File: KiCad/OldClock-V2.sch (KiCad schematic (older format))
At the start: 40 parts, among them J1 FaseCTRL, J2 Screw_Terminal_1x02, J3 Screw_Terminal_1x02, J4 Screw_Terminal_1x02, K1 FINDER-32.21-x300, Q1 Q_NPN_CBE, Q2 Q_PNP_CBE, Q3 Q_PNP_BCE, Q4 Q_NPN_CBE, SW1 Dw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

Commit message: Schematical update
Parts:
- removed K1: FINDER-32.21-x300, Relays_THT:Relay_SPST_Finder_32.21-x300, symbol FINDER-32.21-x300
- added R11: 220R, symbol R
- D7: value LED -> LED_V
- D8: value LED -> LED_R
- Q1: value Q_NPN_CBE -> BC547
- Q2: value Q_PNP_CBE -> BC327
- Q4: value Q_NPN_CBE -> BD410
- R1, R10: value R -> 220R
- R2: value R -> 10k
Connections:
- net +12V: now also J2.2
- net GND: now also Q4.3 (E); no longer Q4.1 (C)
- net at SH1.10 ((*)_10): no longer D8.2 (A)
- net at SH1.11 ((*/MOSI)_11): now also R10.1
- net at SH1.12 ((MISO)_12): no longer R10.1
- net at SH1.13 ((SCK)_13): now also D8.2 (A)
- net at J2.1: now also Q4.1 (C)
- net at Q2.2 (B), R2.1: now also R11.1; no longer Q1.1 (C)
- new net: Q1.1 (C), R11.2
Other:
- moved on the sheet: D8, J2, Q1, Q4, R1, R10, R8
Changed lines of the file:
@@
 LIBS:nxp
 LIBS:dc-dc
-LIBS:OdlClock-V2-cache
+LIBS:OldClock-V2-cache
 EELAYER 25 0
 EELAYER END
@@
 L Q_NPN_CBE Q4
 U 1 1 5A37E50C
-P 8850 1175
-F 0 "Q4" H 9050 1225 50  0000 L CNN
-F 1 "Q_NPN_CBE" H 9050 1125 50  0000 L CNN
-F 2 "" H 9050 1275 50  0001 C CNN
-F 3 "" H 8850 1175 50  0001 C CNN
-	1    8850 1175
+P 8875 1725
+F 0 "Q4" H 9075 1775 50  0000 L CNN
+F 1 "BD410" H 9125 1525 50  0000 L CNN
+F 2 "" H 9075 1825 50  0001 C CNN
+F 3 "" H 8875 1725 50  0001 C CNN
+	1    8875 1725
 	1    0    0    -1
 $EndComp
@@
 L R R10
 U 1 1 5A37E57D
-P 8500 1175
-F 0 "R10" V 8580 1175 50  0000 C CNN
-F 1 "R" V 8500 1175 50  0000 C CNN
-F 2 "" V 8430 1175 50  0001 C CNN
-F 3 "" H 8500 1175 50  0001 C CNN
-	1    8500 1175
+P 8525 1725
+F 0 "R10" V 8605 1725 50  0000 C CNN
+F 1 "220R" V 8525 1725 50  0000 C CNN
+F 2 "" V 8455 1725 50  0001 C CNN
+F 3 "" H 8525 1725 50  0001 C CNN
+	1    8525 1725
 	0    -1   -1   0
 $EndComp
@@
 L GND #PWR29
 U 1 1 5A37E9D1
-P 8950 975
-F 0 "#PWR29" H 8950 725 50  0001 C CNN
-F 1 "GND" H 8950 825 50  0000 C CNN
-F 2 "" H 8950 975 50  0001 C CNN
-F 3 "" H 8950 975 50  0001 C CNN
-	1    8950 975
-	-1   0    0    1
+P 8975 1925
+F 0 "#PWR29" H 8975 1675 50  0001 C CNN
+F 1 "GND" H 8975 1775 50  0000 C CNN
+F 2 "" H 8975 1925 50  0001 C CNN
+F 3 "" H 8975 1925 50  0001 C CNN
+	1    8975 1925
+	1    0    0    -1
 $EndComp
 $Comp
 L +12V #PWR30
 U 1 1 5A37EA62
-P 8950 1975
-F 0 "#PWR30" H 8950 1825 50  0001 C CNN
-F 1 "+12V" H 8950 2115 50  0000 C CNN
-F 2 "" H 8950 1975 50  0001 C CNN
-F 3 "" H 8950 1975 50  0001 C CNN
-	1    8950 1975
-	-1   0    0    1
-$EndComp
-$Comp
-L FINDER-32.21-x300 K1
-U 1 1 5A37FBE9
-P 9150 1675
-F 0 "K1" H 9600 1825 50  0000 L CNN
-F 1 "FINDER-32.21-x300" H 9600 1725 50  0000 L CNN
-F 2 "Relays_THT:Relay_SPST_Finder_32.21-x300" H 10420 1645 50  0001 C CNN
-F 3 "" H 9150 1675 50  0001 C CNN
-	1    9150 1675
-	1    0    0    -1
+P 9650 1100
+F 0 "#PWR30" H 9650 950 50  0001 C CNN
+F 1 "+12V" H 9650 1240 50  0000 C CNN
+F 2 "" H 9650 1100 50  0001 C CNN
+F 3 "" H 9650 1100 50  0001 C CNN
+	1    9650 1100
+	0    -1   -1   0
 $EndComp
 $Comp
 L Screw_Terminal_1x02 J2
 U 1 1 5A380BD8
-P 10550 1650
-F 0 "J2" H 10550 1900 50  0000 C TNN
-F 1 "Screw_Terminal_1x02" V 10400 1650 50  0000 C TNN
-F 2 "" H 10550 1425 50  0001 C CNN
-F 3 "" H 10525 1650 50  0001 C CNN
-	1    10550 1650
+P 9850 1200
+F 0 "J2" H 9850 1450 50  0000 C TNN
+F 1 "Screw_Terminal_1x02" V 9700 1200 50  0000 C TNN
+F 2 "" H 9850 975 50  0001 C CNN
+F 3 "" H 9825 1200 50  0001 C CNN
+	1    9850 1200
 	-1   0    0    1
 $EndComp
-Wire Wire Line
-	10350 1750 10350 2025
-Wire Wire Line
-	10350 2025 9350 2025
-Wire Wire Line
-	9350 2025 9350 1975
-Wire Wire Line
-	9450 1375 10250 1375
-Wire Wire Line
-	10250 1375 10250 1550
-Wire Wire Line
-	10250 1550 10350 1550
 $Comp
 L LED D7
@@
 P 6925 1975
 F 0 "D7" H 6925 2075 50  0000 C CNN
-F 1 "LED" H 6925 1875 50  0000 C CNN
+F 1 "LED_V" H 6925 1875 50  0000 C CNN
 F 2 "" H 6925 1975 50  0001 C CNN
 F 3 "" H 6925 1975 50  0001 C CNN
@@
 L LED D8
 U 1 1 5A381040
-P 7250 1850
-F 0 "D8" H 7250 1950 50  0000 C CNN
-F 1 "LED" H 7250 1750 50  0000 C CNN
-F 2 "" H 7250 1850 50  0001 C CNN
-F 3 "" H 7250 1850 50  0001 C CNN
-	1    7250 1850
+P 7250 1475
+F 0 "D8" H 7250 1575 50  0000 C CNN
+F 1 "LED_R" H 7250 1375 50  0000 C CNN
+F 2 "" H 7250 1475 50  0001 C CNN
+F 3 "" H 7250 1475 50  0001 C CNN
+	1    7250 1475
 	-1   0    0    1
 $EndComp
 Wire Wire Line
-	7100 1850 6775 1850
+	7100 1475 6775 1475
 Wire Wire Line
 	7400 1975 7075 1975
@@
 L R R8
 U 1 1 5A3814AB
-P 7550 1850
-F 0 "R8" V 7630 1850 50  0000 C CNN
-F 1 "R" V 7550 1850 50  0000 C CNN
-F 2 "" V 7480 1850 50  0001 C CNN
-F 3 "" H 7550 1850 50  0001 C CNN
-	1    7550 1850
+P 7550 1475
+F 0 "R8" V 7630 1475 50  0000 C CNN
+F 1 "R" V 7550 1475 50  0000 C CNN
+F 2 "" V 7480 1475 50  0001 C CNN
+F 3 "" H 7550 1475 50  0001 C CNN
+	1    7550 1475
 	0    -1   -1   0
 $EndComp
@@
 	0    -1   -1   0
 $EndComp
-Wire Wire Line
-	7700 1975 7700 1850
 $Comp
 L CONN_01X02 J1
@@
 Text GLabel 6775 2100 2    60   Input ~ 0
 UPS
-Wire Wire Line
-	8350 1175 7200 1175
-Wire Wire Line
-	7200 1175 7200 1600
-Wire Wire Line
-	7200 1600 6775 1600
 $Comp
 L R R3
@@
 P 1875 2250
 F 0 "Q2" H 2075 2300 50  0000 L CNN
-F 1 "Q_PNP_CBE" H 2475 2625 50  0001 L CNN
+F 1 "BC327" H 1675 2400 50  0000 L CNN
 F 2 "" H 2075 2350 50  0001 C CNN
 F 3 "" H 1875 2250 50  0001 C CNN
@@
 L Q_NPN_CBE Q1
 U 1 1 5A875735
-P 1575 2450
-F 0 "Q1" H 1775 2500 50  0000 L CNN
-F 1 "Q_NPN_CBE" H 1300 2875 50  0000 L CNN
-F 2 "" H 1775 2550 50  0001 C CNN
-F 3 "" H 1575 2450 50  0001 C CNN
-	1    1575 2450
+P 1575 2750
+F 0 "Q1" H 1775 2800 50  0000 L CNN
+F 1 "BC547" H 1225 2825 50  0000 L CNN
+F 2 "" H 1775 2850 50  0001 C CNN
+F 3 "" H 1575 2750 50  0001 C CNN
+	1    1575 2750
 	1    0    0    -1
 $EndComp
@@
 P 1525 2250
 F 0 "R2" V 1605 2250 50  0000 C CNN
-F 1 "R" V 1525 2250 50  0000 C CNN
+F 1 "10k" V 1525 2250 50  0000 C CNN
 F 2 "" V 1455 2250 50  0001 C CNN
 F 3 "" H 1525 2250 50  0001 C CNN
@@
 L R R1
 U 1 1 5A875B9C
-P 1225 2450
-F 0 "R1" V 1305 2450 50  0000 C CNN
-F 1 "R" V 1225 2450 50  0000 C CNN
-F 2 "" V 1155 2450 50  0001 C CNN
-F 3 "" H 1225 2450 50  0001 C CNN
-	1    1225 2450
+P 1225 2750
+F 0 "R1" V 1305 2750 50  0000 C CNN
+F 1 "220R" V 1225 2750 50  0000 C CNN
+F 2 "" V 1155 2750 50  0001 C CNN
+F 3 "" H 1225 2750 50  0001 C CNN
+	1    1225 2750
 	0    1    1    0
 $EndComp
@@
 	-1   0    0    1
 $EndComp
-Text GLabel 1075 2450 0    60   Input ~ 0
+Text GLabel 1075 2750 0    60   Input ~ 0
 UPS
 $Comp
 L GND #PWR5
 U 1 1 5A877D92
-P 1675 2650
-F 0 "#PWR5" H 1675 2400 50  0001 C CNN
-F 1 "GND" H 1675 2500 50  0000 C CNN
-F 2 "" H 1675 2650 50  0001 C CNN
-F 3 "" H 1675 2650 50  0001 C CNN
-	1    1675 2650
+P 1675 2950
+F 0 "#PWR5" H 1675 2700 50  0001 C CNN
+F 1 "GND" H 1675 2800 50  0000 C CNN
+F 2 "" H 1675 2950 50  0001 C CNN
+F 3 "" H 1675 2950 50  0001 C CNN
+	1    1675 2950
 	1    0    0    -1
 $EndComp
@@
 	0    -1   -1   0
 $EndComp
+$Comp
+L R R11
+U 1 1 5A9970D4
+P 1675 2400
+F 0 "R11" V 1755 2400 50  0000 C CNN
+F 1 "220R" V 1675 2400 50  0000 C CNN
+F 2 "" V 1605 2400 50  0001 C CNN
+F 3 "" H 1675 2400 50  0001 C CNN
+	1    1675 2400
+	1    0    0    -1
+$EndComp
+$Comp
+L GND #PWR?
+U 1 1 5AA24140
+P 7700 1475
+F 0 "#PWR?" H 7700 1225 50  0001 C CNN
+F 1 "GND" H 7700 1325 50  0000 C CNN
+F 2 "" H 7700 1475 50  0001 C CNN
+F 3 "" H 7700 1475 50  0001 C CNN
+	1    7700 1475
+	0    -1   -1   0
+$EndComp
+Wire Wire Line
+	6775 1725 8375 1725
+Wire Wire Line
+	9650 1300 8975 1300
+Wire Wire Line
+	8975 1300 8975 1525
 $EndSCHEMATC

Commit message: Update for DS3231
Schematical and library update
New eeprom address.
chmage pinout from simulator to final board
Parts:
- U2: value DS1307 -> DS3231
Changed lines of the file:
@@
 LIBS:valves
 LIBS:Altera
-LIBS:Msystem
 LIBS:motor_drivers
-LIBS:79xx-Regler-BuildingBlock_ModB_RevA-cache
-LIBS:Switch
-LIBS:Display
-LIBS:Relay
 LIBS:relays
-LIBS:nxp
 LIBS:dc-dc
 LIBS:OldClock-V2-cache
@@
 P 3575 4650
 F 0 "U2" H 4150 5825 60  0000 C CNN
-F 1 "DS1307" V 4150 5450 60  0000 C CNN
+F 1 "DS3231" V 4150 5450 60  0000 C CNN
 F 2 "" H 3825 4650 60  0001 C CNN
 F 3 "" H 3825 4650 60  0001 C CNN
@@
 F 1 "CAPACITOR_POLARISED_RevE_Date15jun2010" H 2825 2450 30  0001 C CNN
 F 2 "" H 2325 2250 60  0001 C CNN
-F 3 "" H 2325 2250 60  0001 C CNN
+F 3 "Supercap" H 2325 2250 60  0001 C CNN
 	1    2325 2250
 	0    1    1    0

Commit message: KiCad file update
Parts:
- removed C2: 470uF 25V, symbol CAPACITOR_POLARISED_RevE_Date15jun2010
- added C2: 470nF, symbol Device:C
- C1: value CAPACITOR_POLARISED_RevE_Date15jun2010 -> SuperCap 1F; symbol CAPACITOR_POLARISED_RevE_Date15jun2010 -> Device:CP
- C3: symbol C -> Device:CP
- D1: symbol DIODE-STANDARD_RevE_Date15jun2010 -> Device:D
- D2: symbol D_Zener -> Device:D_Zener
- D3, D4, D5, D6: symbol D -> Device:D
- D7, D8: symbol LED -> Device:LED
- J1: symbol CONN_01X02 -> Connector:Conn_01x02_Male
- J2, J3, J4: symbol Screw_Terminal_1x02 -> Connector:Screw_Terminal_01x02
- L1: symbol L -> Device:L
- Q1, Q4: symbol Q_NPN_CBE -> Device:Q_NPN_CBE
- Q2: symbol Q_PNP_CBE -> Device:Q_PNP_CBE
- Q3: symbol Q_PNP_BCE -> Device:Q_PNP_BCE
- R: renamed from 15K1; value R -> 15R; symbol R -> Device:R
- R1, R11, R2, R3, R4, R5, R6: symbol R -> Device:R
- R10: value 220R -> R220; symbol R -> Device:R
- R7: symbol LDR03 -> Sensor_Optical:LDR03
- R8, R9: value R -> 4R7; symbol R -> Device:R
- SH1: value ARDUINO_as_UNO -> Ardu Nano; symbol ARDUINO_as_UNO -> Msystem:ARDUINO_NANO_R3_50mil
- SW1, SW2, SW3: symbol SW_Push -> Switch:SW_Push
- U1: symbol LM2575-5.0BT -> Regulator_Switching:LM2575-5.0BT
- U2: symbol DS1307 -> Msystem:DS1307
- U3: symbol I2c_LCD -> Msystem:I2c_LCD
- U4: symbol L293D -> Driver_Motor:L293D
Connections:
- net +12V: now also J2.1 (Pin_1), J4.2 (Pin_2); no longer J2.2, J4.1
- net +5V: now also SH1.5V
- net GND: now also D1.2 (A), J1.1 (Pin_1), J4.1 (Pin_1), SH1.GND2 (GND/2), SW1.2, SW3.2, C2.2; no longer D1.1 (A), J4.2
- net at SH1.5 ((*)_5): now also J1.2 (Pin_2); no longer J1.1 (P1)
- net at R3.2, R4.1, SH1.A1: now also D2.1 (K)
- net at U2.10 (SDA), U3.2 (SDA): now also SH1.A4 (A4_(SDA)); no longer SH1.A4/1 (A4_(SDA)/1)
- net at U2.11 (SCL), U3.1 (SCL): now also SH1.A5 (A5_(SCL)); no longer SH1.A5/1 (A5_(SCL)/1)
- net at D3.2 (A), D4.1 (K), U4.3 (1Y): now also J3.1 (Pin_1); no longer J3.2
- net at D5.2 (A), D6.1 (K), U4.6 (2Y): now also J3.2 (Pin_2); no longer J3.1
- net at Q4.1 (C): now also J2.2 (Pin_2); no longer J2.1
- net at L1.1, U1.2 (OUT): now also D1.1 (K); no longer D1.2 (K)
- net UPS renamed PPer
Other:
- moved on the sheet: D1, J2, J3, J4, R9, SW1, SW2, SW3, U2

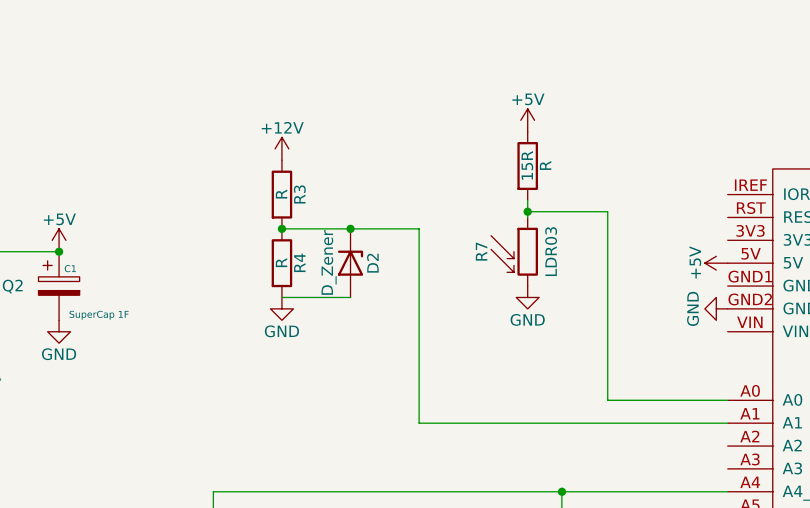
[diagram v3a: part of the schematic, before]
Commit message: Schematical and code update Schematical resistor valude in Vsens code to comment the Vsens Ratio
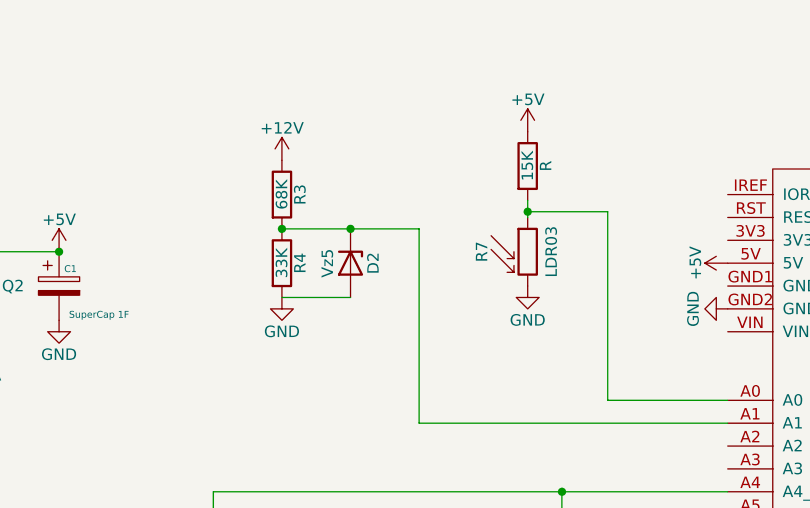
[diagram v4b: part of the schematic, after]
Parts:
- D2: value D_Zener -> Vz5
- R: value 15R -> 15K
- R3: value R -> 68K
- R4: value R -> 33K
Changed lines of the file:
@@
 P 4375 1675
 F 0 "R" V 4455 1675 50  0000 C CNN
-F 1 "15R" V 4375 1675 50  0000 C CNN
+F 1 "15K" V 4375 1675 50  0000 C CNN
 F 2 "" V 4305 1675 50  0001 C CNN
 F 3 "~" H 4375 1675 50  0001 C CNN
@@
 P 3300 1800
 F 0 "R3" V 3380 1800 50  0000 C CNN
-F 1 "R" V 3300 1800 50  0000 C CNN
+F 1 "68K" V 3300 1800 50  0000 C CNN
 F 2 "" V 3230 1800 50  0001 C CNN
 F 3 "" H 3300 1800 50  0001 C CNN
@@
 P 3300 2100
 F 0 "R4" V 3380 2100 50  0000 C CNN
-F 1 "R" V 3300 2100 50  0000 C CNN
+F 1 "33K" V 3300 2100 50  0000 C CNN
 F 2 "" V 3230 2100 50  0001 C CNN
 F 3 "" H 3300 2100 50  0001 C CNN
@@
 P 3600 2100
 F 0 "D2" H 3600 2200 50  0000 C CNN
-F 1 "D_Zener" H 3600 2000 50  0000 C CNN
+F 1 "Vz5" H 3600 2000 50  0000 C CNN
 F 2 "" H 3600 2100 50  0001 C CNN
 F 3 "~" H 3600 2100 50  0001 C CNN
